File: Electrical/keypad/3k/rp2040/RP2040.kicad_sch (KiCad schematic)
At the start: 73 parts, among them J1 Conn_01x04_Socket, P1 USB-TYPE-C-016, Q1 BSS138, SW1 TS-1187A-B-A-B, SW2 TS-1187A-B-A-B, SW3 BUTT1, SW4 BUTT3, SW5 BUTT2, U1 PRTR5V0U2X, U2 ME6208A44M3G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

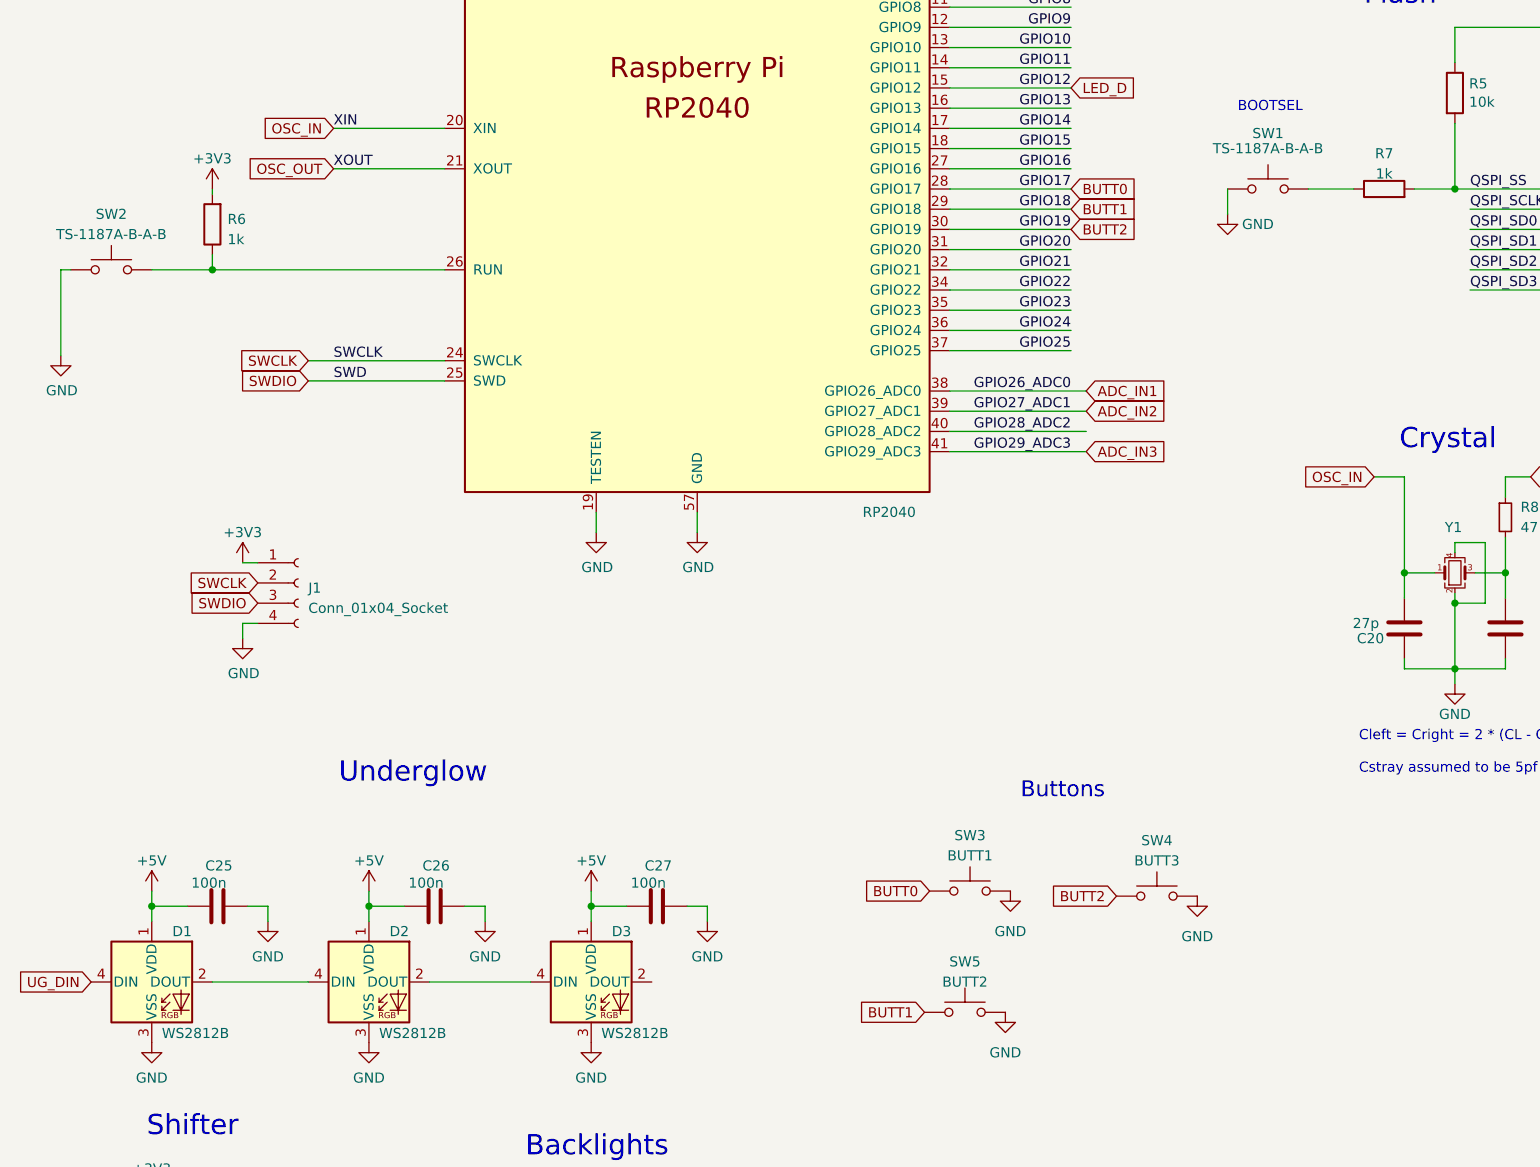
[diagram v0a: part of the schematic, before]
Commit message: fixes rp2040 board, stm32 board still todo
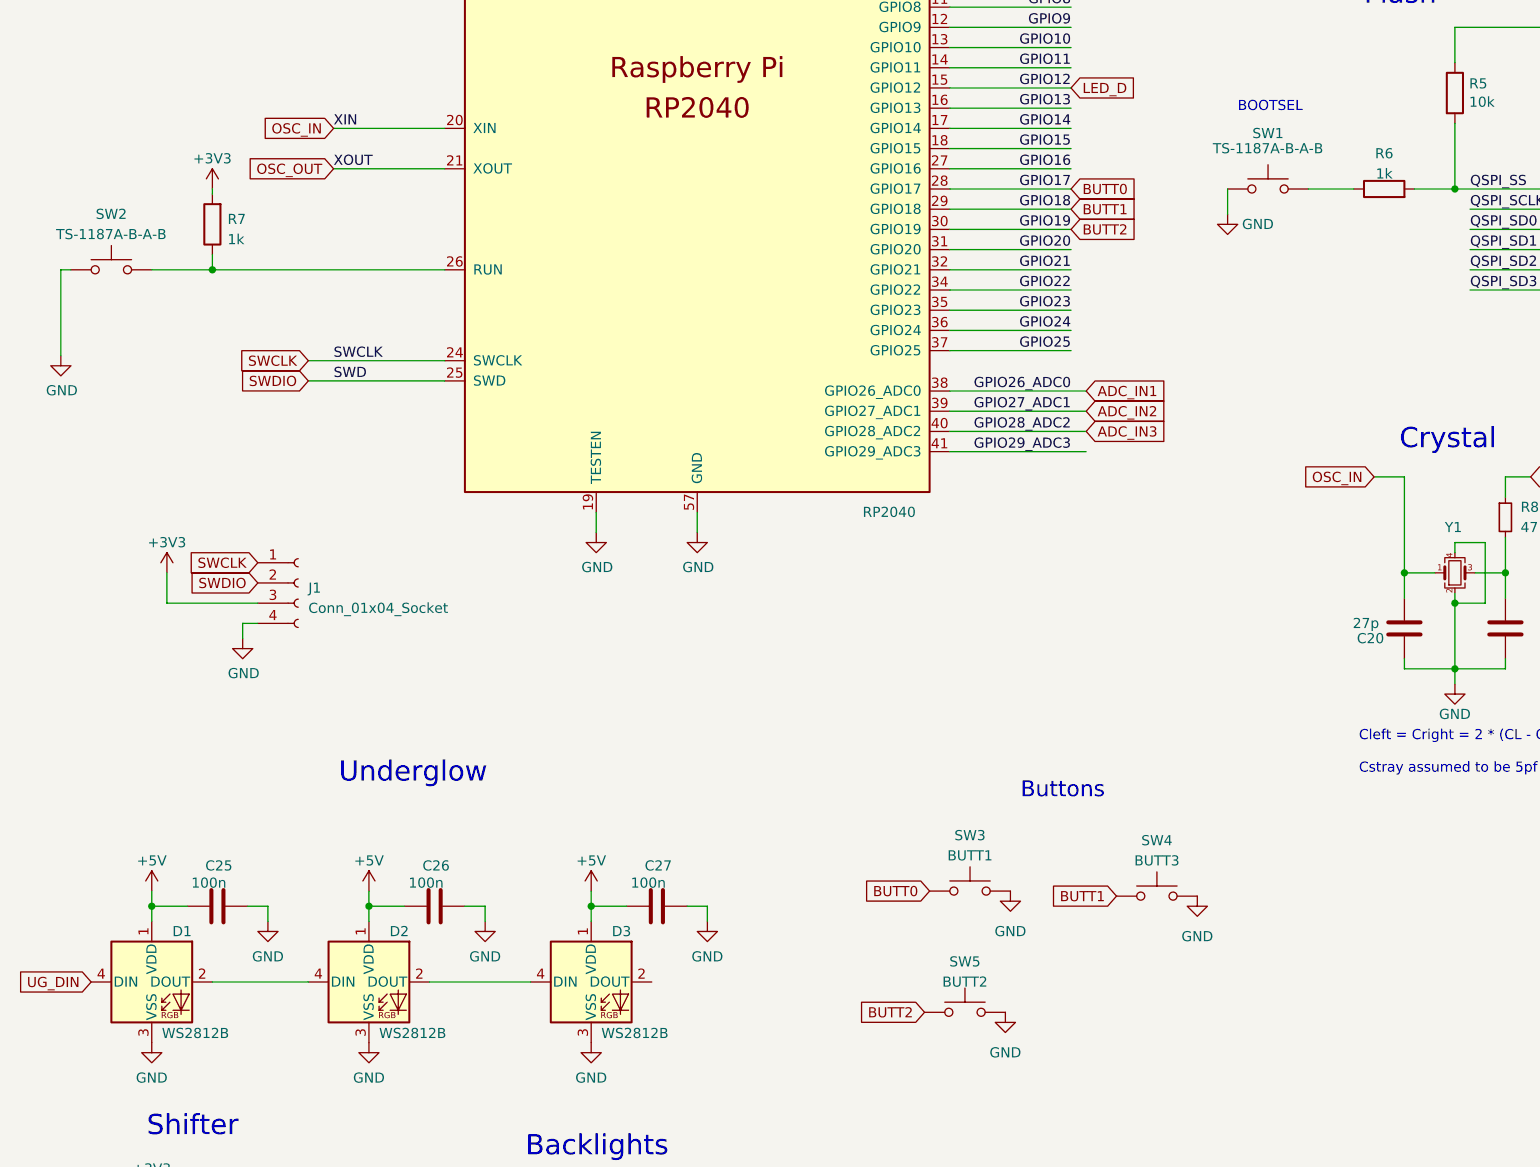
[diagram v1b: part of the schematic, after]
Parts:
- renumbered R7 to R6, R6 to R7
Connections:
- net GPIO28_ADC2 is gone; now on net ADC_IN3: U3.40 (GPIO28_ADC2)
- net +3V3: now also J1.3 (Pin_3); no longer J1.1 (Pin_1)
- net ADC_IN3: no longer U3.41 (GPIO29_ADC3)
- net BUTT1: now also SW4.1; no longer SW5.1
- net BUTT2: now also SW5.1; no longer SW4.1
- net SWCLK: now also J1.1 (Pin_1); no longer J1.2 (Pin_2)
- net SWDIO: now also J1.2 (Pin_2); no longer J1.3 (Pin_3)
- new net GPIO29_ADC3: U3.41 (GPIO29_ADC3)

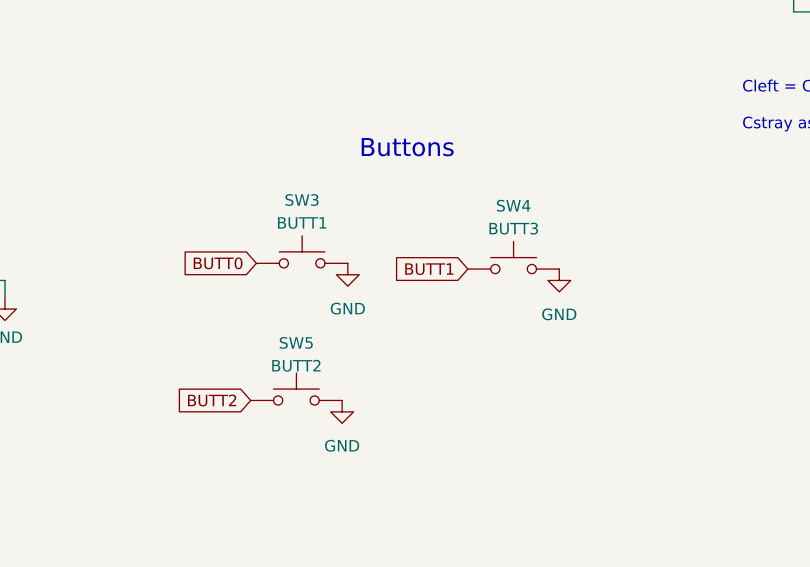
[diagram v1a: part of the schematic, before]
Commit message: adds stitching vias
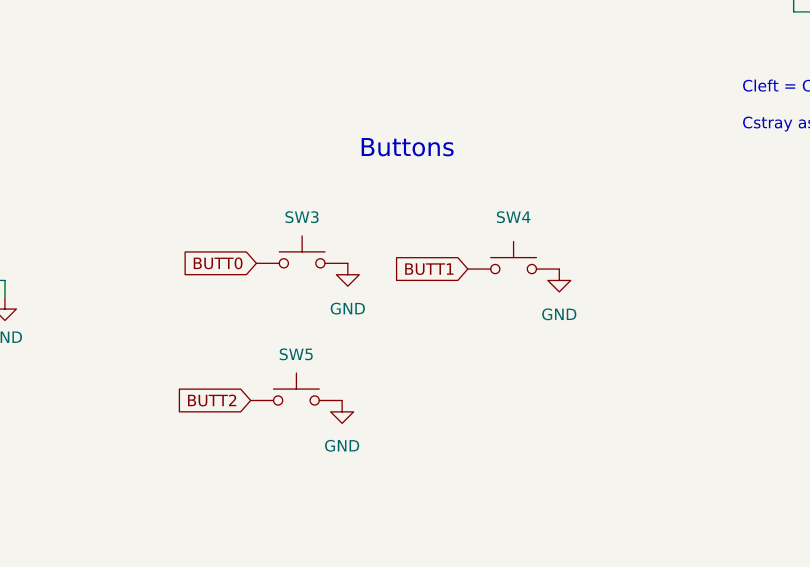
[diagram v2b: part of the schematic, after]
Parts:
- SW4: value BUTT3 -> BUTT2
- SW5: value BUTT2 -> BUTT3
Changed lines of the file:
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@@
   (symbol (lib_id "Switch:SW_Push") (at 133.35 228.6 0) (unit 1)
     (in_bom yes) (on_board yes) (dnp no) (fields_autoplaced)
-    (property "Reference" "SW5" (at 133.35 222.25 0)
-      (effects (font (size 1.27 1.27)))
-    )
-    (property "Value" "BUTT2" (at 133.35 224.79 0)
-      (effects (font (size 1.27 1.27)))
+    (property "Reference" "SW5" (at 133.35 223.52 0)
+      (effects (font (size 1.27 1.27)))
+    )
+    (property "Value" "BUTT3" (at 133.35 224.79 0)
+      (effects (font (size 1.27 1.27)) hide)
     )
     (property "Footprint" "Button_Switch_SMD:SW_Push_1P1T_NO_6x6mm_H9.5mm" (at 133.35 223.52 0)
@@
   (symbol (lib_id "Switch:SW_Push") (at 157.48 213.995 0) (unit 1)
     (in_bom yes) (on_board yes) (dnp no) (fields_autoplaced)
-    (property "Reference" "SW4" (at 157.48 207.01 0)
-      (effects (font (size 1.27 1.27)))
-    )
-    (property "Value" "BUTT3" (at 157.48 209.55 0)
-      (effects (font (size 1.27 1.27)))
+    (property "Reference" "SW4" (at 157.48 208.28 0)
+      (effects (font (size 1.27 1.27)))
+    )
+    (property "Value" "BUTT2" (at 157.48 208.28 0)
+      (effects (font (size 1.27 1.27)) hide)
     )
     (property "Footprint" "Button_Switch_SMD:SW_Push_1P1T_NO_6x6mm_H9.5mm" (at 157.48 208.915 0)
@@
   (symbol (lib_id "Switch:SW_Push") (at 133.985 213.36 0) (unit 1)
     (in_bom yes) (on_board yes) (dnp no) (fields_autoplaced)
-    (property "Reference" "SW3" (at 133.985 206.375 0)
+    (property "Reference" "SW3" (at 133.985 208.28 0)
       (effects (font (size 1.27 1.27)))
     )
     (property "Value" "BUTT1" (at 133.985 208.915 0)
-      (effects (font (size 1.27 1.27)))
+      (effects (font (size 1.27 1.27)) hide)
     )
     (property "Footprint" "Button_Switch_SMD:SW_Push_1P1T_NO_6x6mm_H9.5mm" (at 133.985 208.28 0)
